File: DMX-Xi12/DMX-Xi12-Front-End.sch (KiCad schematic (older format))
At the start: 14 parts

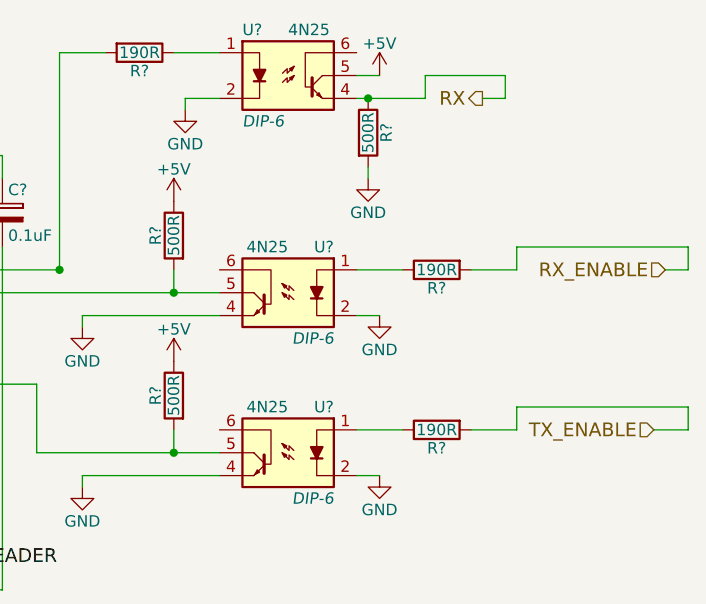
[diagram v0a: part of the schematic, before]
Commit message: added output stage
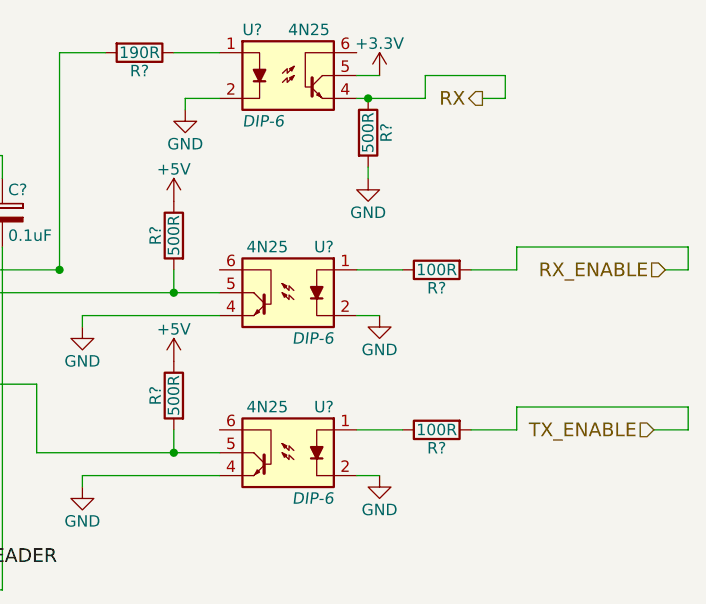
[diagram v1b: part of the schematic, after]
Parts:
- R? (x2): value 190R -> 100R
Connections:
- net +5V: no longer U?.5
- new net +3V3: U?.5
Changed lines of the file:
@@
 LIBS:valves
 LIBS:DMX-Xi12
+LIBS:dips-s
+LIBS:MyPower
 LIBS:DMX-Xi12-cache
 EELAYER 25 0
@@
 $Descr A4 11693 8268
 encoding utf-8
-Sheet 2 3
+Sheet 2 10
 Title "DMX-Xi12 Front End"
 Date ""
@@
 $EndComp
 $Comp
-L +5V #PWR?
-U 1 1 56ADBC0F
-P 5000 4000
-F 0 "#PWR?" H 5000 3850 50  0001 C CNN
-F 1 "+5V" H 5000 4140 50  0000 C CNN
-F 2 "" H 5000 4000 50  0000 C CNN
-F 3 "" H 5000 4000 50  0000 C CNN
-	1    5000 4000
-	1    0    0    -1
-$EndComp
-$Comp
 L R R?
 U 1 1 56ADBC15
@@
 P 8500 3000
 F 0 "R?" V 8580 3000 50  0000 C CNN
-F 1 "190R" V 8500 3000 50  0000 C CNN
+F 1 "100R" V 8500 3000 50  0000 C CNN
 F 2 "" V 8430 3000 50  0000 C CNN
 F 3 "" H 8500 3000 50  0000 C CNN
@@
 $EndComp
 $Comp
-L +5V #PWR?
-U 1 1 56ADBC4A
-P 8250 2150
-F 0 "#PWR?" H 8250 2000 50  0001 C CNN
-F 1 "+5V" H 8250 2290 50  0000 C CNN
-F 2 "" H 8250 2150 50  0000 C CNN
-F 3 "" H 8250 2150 50  0000 C CNN
-	1    8250 2150
-	1    0    0    -1
-$EndComp
-$Comp
 L CP C?
 U 1 1 56ADBC51
@@
 P 8500 3700
 F 0 "R?" V 8580 3700 50  0000 C CNN
-F 1 "190R" V 8500 3700 50  0000 C CNN
+F 1 "100R" V 8500 3700 50  0000 C CNN
 F 2 "" V 8430 3700 50  0000 C CNN
 F 3 "" H 8500 3700 50  0000 C CNN
@@
 	1    0    0    -1
 $EndComp
-Connection ~ 6450 2500
-Wire Wire Line
-	6600 2500 6450 2500
-Wire Wire Line
-	6600 2600 6600 2500
-Wire Wire Line
-	6600 4400 6600 2900
-Connection ~ 5700 4400
-Wire Wire Line
-	5250 4400 6600 4400
-Wire Wire Line
-	5250 4350 5250 4400
-Connection ~ 5250 4000
-Wire Wire Line
-	5250 4050 5250 4000
-Wire Wire Line
-	5700 4200 5700 4450
-Wire Wire Line
-	6950 3250 6950 3200
-Wire Wire Line
-	6850 3000 6300 3000
-Connection ~ 8200 2250
-Wire Wire Line
-	8150 2150 8250 2150
-Connection ~ 6850 3000
-Wire Wire Line
-	8150 2250 8450 2250
-Wire Wire Line
-	6850 2050 6850 3000
-Wire Wire Line
-	8650 3000 8850 3000
-Wire Wire Line
-	8350 3000 8150 3000
-Wire Wire Line
-	6950 3200 7550 3200
-Wire Wire Line
-	7050 2050 6850 2050
-Wire Wire Line
-	6150 2850 6150 3550
-Wire Wire Line
-	6450 2800 6300 2800
-Wire Wire Line
-	6450 2450 6450 2800
-Wire Wire Line
-	6450 3700 6300 3700
-Wire Wire Line
-	6450 3000 6450 3700
-Wire Wire Line
-	5000 4000 5300 4000
-Connection ~ 6450 3000
-Wire Wire Line
-	7350 2050 7550 2050
-Wire Wire Line
-	7400 2300 7400 2250
-Wire Wire Line
-	7400 2250 7550 2250
-Wire Wire Line
-	6300 3100 7550 3100
-Wire Wire Line
-	8200 2600 8200 2550
-Wire Wire Line
-	8250 3200 8150 3200
-Wire Wire Line
-	7350 3000 7350 3100
-Connection ~ 7350 3100
-Wire Wire Line
-	6950 3950 6950 3900
-Wire Wire Line
-	8650 3700 8850 3700
-Wire Wire Line
-	8350 3700 8150 3700
-Wire Wire Line
-	6950 3900 7550 3900
-Wire Wire Line
-	8250 3900 8150 3900
-Wire Wire Line
-	7350 3700 7350 3800
-Connection ~ 7350 3800
-Wire Wire Line
-	6750 3800 7550 3800
-Wire Wire Line
-	6750 3800 6750 3500
-Wire Wire Line
-	6750 3500 6300 3500
-Wire Wire Line
-	6300 3300 6300 3200
-Wire Wire Line
-	5200 3000 5200 2900
-Wire Wire Line
-	5200 2900 5300 2900
-Wire Wire Line
-	4150 3000 5200 3000
-Wire Wire Line
-	5300 3100 4150 3100
-Wire Wire Line
-	3600 3250 3600 3200
-Wire Wire Line
-	3600 3200 3350 3200
-Wire Wire Line
-	3350 3200 3350 3300
-Wire Wire Line
-	3600 2150 3600 2100
-Wire Wire Line
-	3600 2100 3350 2100
-Wire Wire Line
-	3350 2100 3350 2200
-Wire Wire Line
-	4150 4100 4350 4100
-Wire Wire Line
-	4350 4100 4350 3600
-Wire Wire Line
-	4350 3600 5300 3600
-Wire Wire Line
-	4150 4200 4450 4200
-Wire Wire Line
-	4450 4200 4450 3800
-Wire Wire Line
-	4450 3800 5300 3800
 Text Label 6300 4300 0    60   ~ 0
 SRL_HEADER
-Wire Wire Line
-	6300 3900 6300 4300
 $Comp
 L GND #PWR?
@@
 F 3 "" H 6300 4700 50  0000 C CNN
 	1    6300 4700
+	1    0    0    -1
+$EndComp
+Text Label 6600 4700 0    60   ~ 0
+SRL_HEADER_+
+Text Label 6300 4550 0    60   ~ 0
+SRL_HEADER-
+Text HLabel 9500 3000 0    60   Input ~ 0
+RX_ENABLE
+Text HLabel 9450 3700 0    60   Input ~ 0
+TX_ENABLE
+Text HLabel 8700 2250 0    60   Output ~ 0
+RX
+Connection ~ 6450 2500
+Wire Wire Line
+	6600 2500 6450 2500
+Wire Wire Line
+	6600 2600 6600 2500
+Wire Wire Line
+	6600 4400 6600 2900
+Connection ~ 5700 4400
+Wire Wire Line
+	5250 4400 6600 4400
+Wire Wire Line
+	5250 4350 5250 4400
+Connection ~ 5250 4000
+Wire Wire Line
+	5250 4050 5250 4000
+Wire Wire Line
+	5700 4200 5700 4450
+Wire Wire Line
+	6950 3250 6950 3200
+Wire Wire Line
+	6850 3000 6300 3000
+Connection ~ 8200 2250
+Wire Wire Line
+	8150 2150 8250 2150
+Connection ~ 6850 3000
+Wire Wire Line
+	8150 2250 8450 2250
+Wire Wire Line
+	6850 2050 6850 3000
+Wire Wire Line
+	8650 3000 8850 3000
+Wire Wire Line
+	8350 3000 8150 3000
+Wire Wire Line
+	6950 3200 7550 3200
+Wire Wire Line
+	7050 2050 6850 2050
+Wire Wire Line
+	6150 2850 6150 3550
+Wire Wire Line
+	6450 2800 6300 2800
+Wire Wire Line
+	6450 2450 6450 2800
+Wire Wire Line
+	6450 3700 6300 3700
+Wire Wire Line
+	6450 3000 6450 3700
+Wire Wire Line
+	5000 4000 5300 4000
+Connection ~ 6450 3000
+Wire Wire Line
+	7350 2050 7550 2050
+Wire Wire Line
+	7400 2300 7400 2250
+Wire Wire Line
+	7400 2250 7550 2250
+Wire Wire Line
+	6300 3100 7550 3100
+Wire Wire Line
+	8200 2600 8200 2550
+Wire Wire Line
+	8250 3200 8150 3200
+Wire Wire Line
+	7350 3000 7350 3100
+Connection ~ 7350 3100
+Wire Wire Line
+	6950 3950 6950 3900
+Wire Wire Line
+	8650 3700 8850 3700
+Wire Wire Line
+	8350 3700 8150 3700
+Wire Wire Line
+	6950 3900 7550 3900
+Wire Wire Line
+	8250 3900 8150 3900
+Wire Wire Line
+	7350 3700 7350 3800
+Connection ~ 7350 3800
+Wire Wire Line
+	6750 3800 7550 3800
+Wire Wire Line
+	6750 3800 6750 3500
+Wire Wire Line
+	6750 3500 6300 3500
+Wire Wire Line
+	6300 3300 6300 3200
+Wire Wire Line
+	5200 3000 5200 2900
+Wire Wire Line
+	5200 2900 5300 2900
+Wire Wire Line
+	4150 3000 5200 3000
+Wire Wire Line
+	5300 3100 4150 3100
+Wire Wire Line
+	3600 3250 3600 3200
+Wire Wire Line
+	3600 3200 3350 3200
+Wire Wire Line
+	3350 3200 3350 3300
+Wire Wire Line
+	3600 2150 3600 2100
+Wire Wire Line
+	3600 2100 3350 2100
+Wire Wire Line
+	3350 2100 3350 2200
+Wire Wire Line
+	4150 4100 4350 4100
+Wire Wire Line
+	4350 4100 4350 3600
+Wire Wire Line
+	4350 3600 5300 3600
+Wire Wire Line
+	4150 4200 4450 4200
+Wire Wire Line
+	4450 4200 4450 3800
+Wire Wire Line
+	4450 3800 5300 3800
+Wire Wire Line
+	6300 3900 6300 4300
+Wire Wire Line
+	6300 4700 6300 4550
+Wire Wire Line
+	9500 3000 9600 3000
+Wire Wire Line
+	9600 3000 9600 2900
+Wire Wire Line
+	9600 2900 8850 2900
+Wire Wire Line
+	8850 2900 8850 3000
+Wire Wire Line
+	9450 3700 9600 3700
+Wire Wire Line
+	9600 3700 9600 3600
+Wire Wire Line
+	9600 3600 8850 3600
+Wire Wire Line
+	8850 3600 8850 3700
+Wire Wire Line
+	8700 2250 8800 2250
+Wire Wire Line
+	8800 2250 8800 2150
+Wire Wire Line
+	8800 2150 8450 2150
+Wire Wire Line
+	8450 2150 8450 2250
+$Comp
+L +5V #PWR?
+U 1 1 56ADBC0F
+P 5000 4000
+F 0 "#PWR?" H 5000 3850 50  0001 C CNN
+F 1 "+5V" H 5000 4140 50  0000 C CNN
+F 2 "" H 5000 4000 50  0000 C CNN
+F 3 "" H 5000 4000 50  0000 C CNN
+	1    5000 4000
+	1    0    0    -1
+$EndComp
+$Comp
+L +3.3V #PWR?
+U 1 1 56B588CC
+P 8250 2150
+F 0 "#PWR?" H 8250 2000 50  0001 C CNN
+F 1 "+3.3V" H 8250 2290 50  0000 C CNN
+F 2 "" H 8250 2150 50  0000 C CNN
+F 3 "" H 8250 2150 50  0000 C CNN
+	1    8250 2150
 	1    0    0    -1
 $EndComp
@@
 	-1   0    0    1
 $EndComp
-Text Label 6600 4700 0    60   ~ 0
-SRL_HEADER_+
-Text Label 6300 4550 0    60   ~ 0
-SRL_HEADER-
-Wire Wire Line
-	6300 4700 6300 4550
-Text HLabel 9500 3000 0    60   Input ~ 0
-RX_ENABLE
-Wire Wire Line
-	9500 3000 9600 3000
-Wire Wire Line
-	9600 3000 9600 2900
-Wire Wire Line
-	9600 2900 8850 2900
-Wire Wire Line
-	8850 2900 8850 3000
-Text HLabel 9450 3700 0    60   Input ~ 0
-TX_ENABLE
-Wire Wire Line
-	9450 3700 9600 3700
-Wire Wire Line
-	9600 3700 9600 3600
-Wire Wire Line
-	9600 3600 8850 3600
-Wire Wire Line
-	8850 3600 8850 3700
-Text HLabel 8700 2250 0    60   Output ~ 0
-RX
-Wire Wire Line
-	8700 2250 8800 2250
-Wire Wire Line
-	8800 2250 8800 2150
-Wire Wire Line
-	8800 2150 8450 2150
-Wire Wire Line
-	8450 2150 8450 2250
 $EndSCHEMATC

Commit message: made dlaw changes etc
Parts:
- removed R?: 190R, symbol R
- removed R? (x3): 500R, symbol R
- removed R? (x2): 100R, symbol R
- removed U? (x3): 4N25, DIP-6, symbol 4N25
- added SW?: Switch_SPDT_x2, symbol Switch_SPDT_x2
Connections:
- net labels removed: SRL_HEADER, SRL_HEADER-, SRL_HEADER_+
- wire segments 69 -> 38

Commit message: working on pcb
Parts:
- C1, C2: renamed from C?; footprint (none) -> Capacitors_SMD:C_0603
- J1, J2: renamed from J?; footprint (none) -> Connect:RJ45_8
- SW1: renamed from SW?; footprint (none) -> Connect:GS3
- U1: renamed from U?; footprint TSSOP-14EP -> Housings_SSOP:TSSOP-14_4.4x5mm_Pitch0.65mm
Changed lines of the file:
@@
 $EndDescr
 $Comp
-L MAX13450E U?
+L MAX13450E U1
 U 1 1 56ADBBFC
 P 5800 3400
-F 0 "U?" H 5500 4150 50  0000 C CNN
+F 0 "U1" H 5500 4150 50  0000 C CNN
 F 1 "MAX13450E" H 5950 4150 50  0000 C CNN
-F 2 "TSSOP-14EP" H 5700 4000 50  0001 C CNN
+F 2 "Housings_SSOP:TSSOP-14_4.4x5mm_Pitch0.65mm" H 5700 4000 50  0001 C CNN
 F 3 "" H 5825 3300 50  0000 C CNN
 	1    5800 3400
@@
 $EndComp
 $Comp
-L GND #PWR?
+L GND #PWR01
 U 1 1 56ADBC03
 P 5700 4450
-F 0 "#PWR?" H 5700 4200 50  0001 C CNN
+F 0 "#PWR01" H 5700 4200 50  0001 C CNN
 F 1 "GND" H 5700 4300 50  0000 C CNN
 F 2 "" H 5700 4450 50  0000 C CNN
@@
 $EndComp
 $Comp
-L +5V #PWR?
+L +5V #PWR02
 U 1 1 56ADBC09
 P 6450 2450
-F 0 "#PWR?" H 6450 2300 50  0001 C CNN
+F 0 "#PWR02" H 6450 2300 50  0001 C CNN
 F 1 "+5V" H 6450 2590 50  0000 C CNN
 F 2 "" H 6450 2450 50  0000 C CNN
@@
 $EndComp
 $Comp
-L CP C?
+L CP C1
 U 1 1 56ADBC51
 P 5250 4200
-F 0 "C?" H 5275 4300 50  0000 L CNN
+F 0 "C1" H 5275 4300 50  0000 L CNN
 F 1 "0.1uF" H 5275 4100 50  0000 L CNN
-F 2 "" H 5288 4050 50  0000 C CNN
+F 2 "Capacitors_SMD:C_0603" H 5288 4050 50  0001 C CNN
 F 3 "" H 5250 4200 50  0000 C CNN
 	1    5250 4200
@@
 $EndComp
 $Comp
-L CP C?
+L CP C2
 U 1 1 56ADBC58
 P 6600 2750
-F 0 "C?" H 6625 2850 50  0000 L CNN
+F 0 "C2" H 6625 2850 50  0000 L CNN
 F 1 "0.1uF" H 6625 2650 50  0000 L CNN
-F 2 "" H 6638 2600 50  0000 C CNN
+F 2 "Capacitors_SMD:C_0603" H 6638 2600 50  0001 C CNN
 F 3 "" H 6600 2750 50  0000 C CNN
 	1    6600 2750
@@
 $EndComp
 $Comp
-L GND #PWR?
+L GND #PWR03
 U 1 1 56ADBC9B
 P 6300 3300
-F 0 "#PWR?" H 6300 3050 50  0001 C CNN
+F 0 "#PWR03" H 6300 3050 50  0001 C CNN
 F 1 "GND" H 6300 3150 50  0000 C CNN
 F 2 "" H 6300 3300 50  0000 C CNN
@@
 $EndComp
 $Comp
-L RJ45 J?
+L RJ45 J1
 U 1 1 56ADBCA1
 P 3700 2750
-F 0 "J?" H 3900 3250 50  0000 C CNN
+F 0 "J1" H 3900 3250 50  0000 C CNN
 F 1 "RJ45" H 3550 3250 50  0000 C CNN
-F 2 "" H 3700 2750 50  0000 C CNN
+F 2 "Connect:RJ45_8" H 3700 2750 50  0001 C CNN
 F 3 "" H 3700 2750 50  0000 C CNN
 	1    3700 2750
@@
 $EndComp
 $Comp
-L GND #PWR?
+L GND #PWR04
 U 1 1 56ADBCA8
 P 3600 2150
-F 0 "#PWR?" H 3600 1900 50  0001 C CNN
+F 0 "#PWR04" H 3600 1900 50  0001 C CNN
 F 1 "GND" H 3600 2000 50  0000 C CNN
 F 2 "" H 3600 2150 50  0000 C CNN
@@
 $EndComp
 $Comp
-L RJ45 J?
+L RJ45 J2
 U 1 1 56ADBCAE
 P 3700 3850
-F 0 "J?" H 3900 4350 50  0000 C CNN
+F 0 "J2" H 3900 4350 50  0000 C CNN
 F 1 "RJ45" H 3550 4350 50  0000 C CNN
-F 2 "" H 3700 3850 50  0000 C CNN
+F 2 "Connect:RJ45_8" H 3700 3850 50  0001 C CNN
 F 3 "" H 3700 3850 50  0000 C CNN
 	1    3700 3850
@@
 $EndComp
 $Comp
-L GND #PWR?
+L GND #PWR05
 U 1 1 56ADBCB5
 P 3600 3250
-F 0 "#PWR?" H 3600 3000 50  0001 C CNN
+F 0 "#PWR05" H 3600 3000 50  0001 C CNN
 F 1 "GND" H 3600 3100 50  0000 C CNN
 F 2 "" H 3600 3250 50  0000 C CNN
@@
 	4450 3800 5300 3800
 $Comp
-L +5V #PWR?
+L +5V #PWR06
 U 1 1 56ADBC0F
 P 5000 4000
-F 0 "#PWR?" H 5000 3850 50  0001 C CNN
+F 0 "#PWR06" H 5000 3850 50  0001 C CNN
 F 1 "+5V" H 5000 4140 50  0000 C CNN
 F 2 "" H 5000 4000 50  0000 C CNN
@@
 	6300 3000 6800 3000
 $Comp
-L Switch_SPDT_x2 SW?
+L Switch_SPDT_x2 SW1
 U 1 1 56DA47FE
 P 7100 3900
-F 0 "SW?" H 6900 4050 50  0000 C CNN
+F 0 "SW1" H 6900 4050 50  0000 C CNN
 F 1 "Switch_SPDT_x2" H 7050 3700 50  0000 C CNN
-F 2 "" H 7100 3900 50  0000 C CNN
+F 2 "Connect:GS3" H 7100 3900 50  0001 C CNN
 F 3 "" H 7100 3900 50  0000 C CNN
 	1    7100 3900
@@
 	6800 3900 6300 3900
 $Comp
-L +3.3V #PWR?
+L +3.3V #PWR07
 U 1 1 56DA48E8
 P 7450 3700
-F 0 "#PWR?" H 7450 3550 50  0001 C CNN
+F 0 "#PWR07" H 7450 3550 50  0001 C CNN
 F 1 "+3.3V" H 7450 3840 50  0000 C CNN
 F 2 "" H 7450 3700 50  0000 C CNN
@@
 	7450 3800 7400 3800
 $Comp
-L GND #PWR?
+L GND #PWR08
 U 1 1 56DA4936
 P 7450 4050
-F 0 "#PWR?" H 7450 3800 50  0001 C CNN
+F 0 "#PWR08" H 7450 3800 50  0001 C CNN
 F 1 "GND" H 7450 3900 50  0000 C CNN
 F 2 "" H 7450 4050 50  0000 C CNN

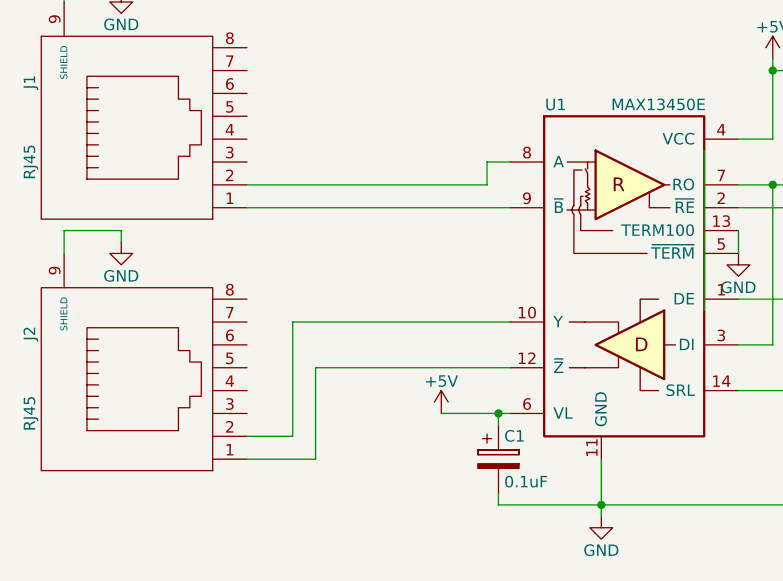
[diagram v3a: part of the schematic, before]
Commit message: completed board. Schematic, is correct but some part values and numbers need updating! Do not trust the schematic yet
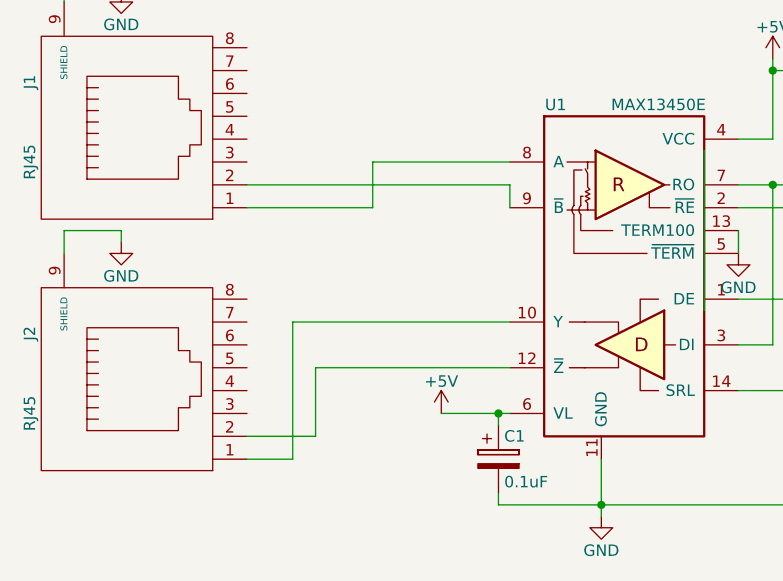
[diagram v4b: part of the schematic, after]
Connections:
- wire segments 38 -> 39
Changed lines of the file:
@@
 	6300 3300 6300 3200
 Wire Wire Line
-	5200 3000 5200 2900
-Wire Wire Line
-	5200 2900 5300 2900
-Wire Wire Line
-	4150 3000 5200 3000
-Wire Wire Line
-	5300 3100 4150 3100
+	4700 2900 5300 2900
 Wire Wire Line
 	3600 3250 3600 3200
@@
 	3350 2100 3350 2200
 Wire Wire Line
-	4150 4100 4350 4100
-Wire Wire Line
-	4350 4100 4350 3600
-Wire Wire Line
 	4350 3600 5300 3600
-Wire Wire Line
-	4150 4200 4450 4200
-Wire Wire Line
-	4450 4200 4450 3800
 Wire Wire Line
 	4450 3800 5300 3800
@@
 Wire Wire Line
 	7450 4000 7400 4000
+Wire Wire Line
+	4700 2900 4700 3100
+Wire Wire Line
+	4700 3100 4150 3100
+Wire Wire Line
+	4150 3000 5300 3000
+Wire Wire Line
+	4350 3600 4350 4200
+Wire Wire Line
+	4350 4200 4150 4200
+Wire Wire Line
+	4450 3800 4450 4100
+Wire Wire Line
+	4450 4100 4150 4100
+Wire Wire Line
+	5300 3000 5300 3100
 $EndSCHEMATC
